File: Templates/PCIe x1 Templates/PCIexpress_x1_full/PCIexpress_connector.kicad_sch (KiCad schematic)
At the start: 2 parts, among them J1 PCIexpress_bracket, J2 PCIexpress_x1

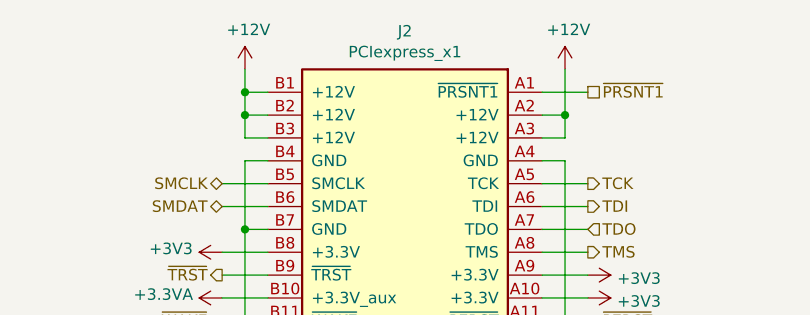
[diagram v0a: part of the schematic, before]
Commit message: Updated PCIe Symbols
fixed pins on all PCIe Symbols input and output are the perspective of the card.
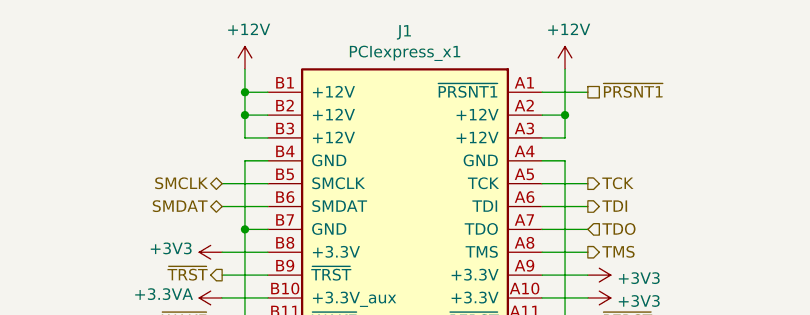
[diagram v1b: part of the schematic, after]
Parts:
- renumbered J2 to J1
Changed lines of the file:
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@@
 		(on_board yes)
 		(dnp no)
-		(property "Reference" "J2"
+		(property "Reference" "J1"
 			(at 105.41 18.6182 0)
 			(effects
@@
 			(project ""
 				(path "/d4a655a4-a1b2-4c75-b7b5-cc7400a5115b/00000000-0000-0000-0000-00005d508b15"
-					(reference "J2")
+					(reference "J1")
 					(unit 1)
 				)

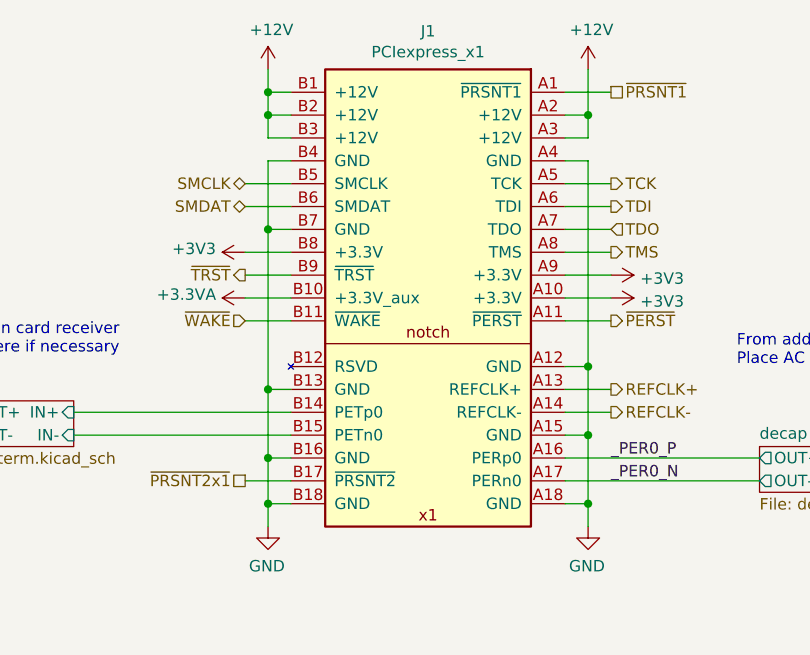
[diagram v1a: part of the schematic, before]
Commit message: updated names on symbols
updated the "Value" field in the m.2 symbols so the name of the connector is shown in your schematic.

updated a few templates with new m.2 symbols
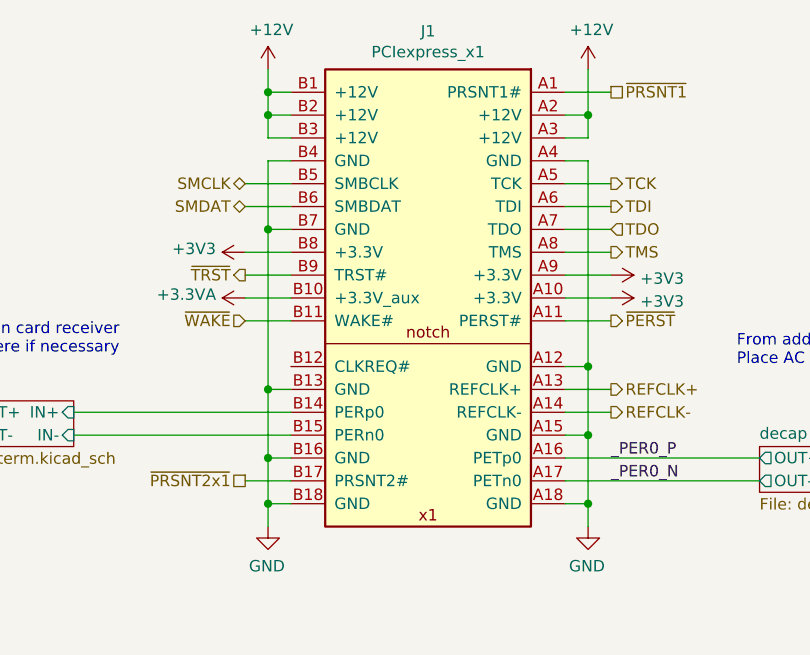
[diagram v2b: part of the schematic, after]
